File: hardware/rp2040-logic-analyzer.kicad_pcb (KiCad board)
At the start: 4 copper layers, 65 x 45 mm, 82 parts, among them J1 TYPE-C-31-M-12, J2 PROBE 2x16, J3 VREF_EXT, J4 ADC 1x3 (DNF), SW1 SK13D07VG5, SW2 TS-1187A-B-A-B, SW3 TS-1187A-B-A-B, U1 RP2040, U2 W25Q128JVSIQ, U3 TXU0104PWR, U4 TXU0104PWR, U5 TXU0104PWR, U6 TXU0104PWR, U7 AMS1117-3.3, U8 USBLC6-2SC6, X1 ABM8-272-T3 12MHz

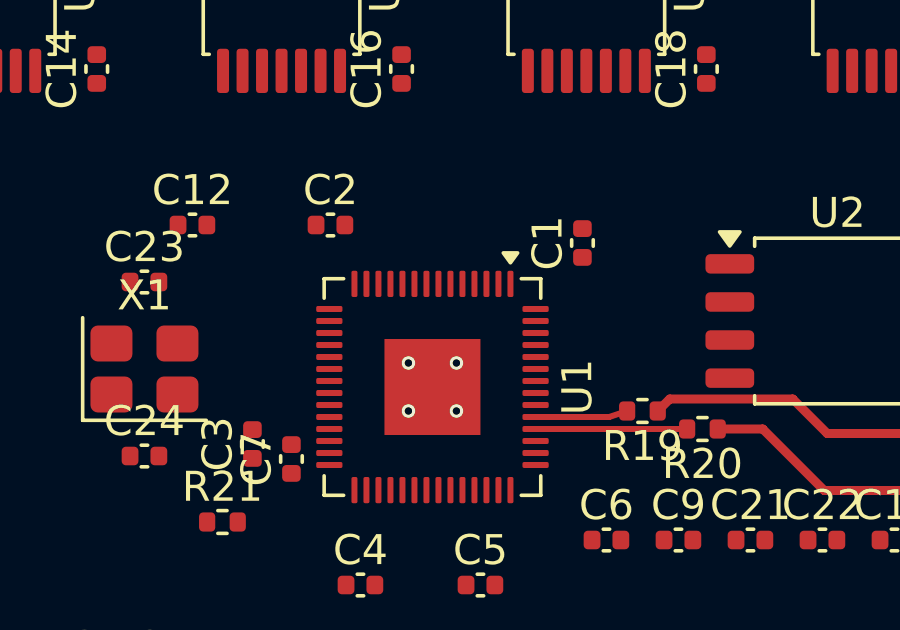
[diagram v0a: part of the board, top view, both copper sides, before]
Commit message: 人間の GUI 編集を取り込み（PCB: 微細ピッチのファンアウト配線 10 本＋ビア 5・回路図の整形）
Co-Authored-By: Claude Opus 5 (1M context) <noreply@anthropic.com>
Claude-Session: https://claude.ai/code/session_01QcyfLK5Dm75FgDGZMr6fff
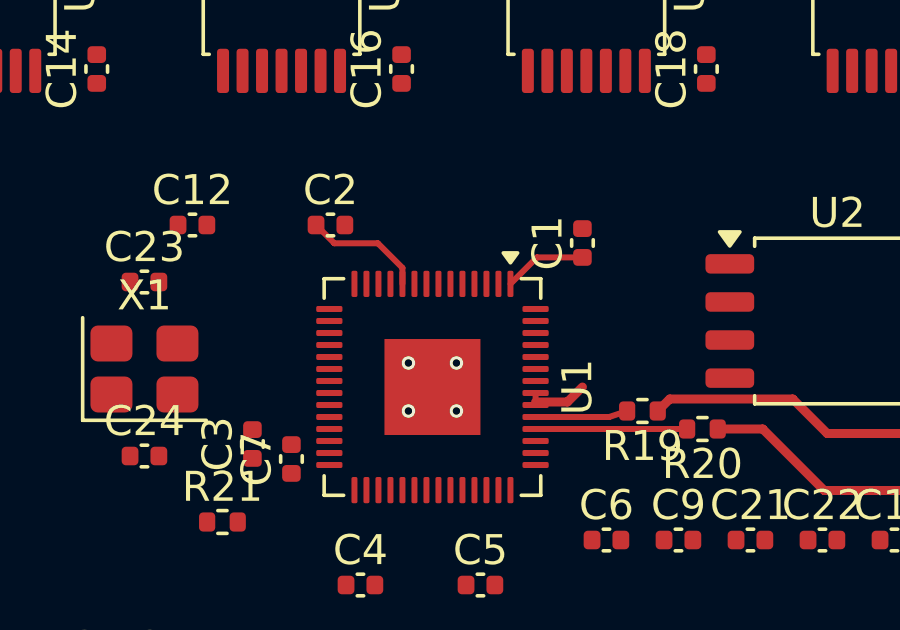
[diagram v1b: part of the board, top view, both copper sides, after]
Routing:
- net +3V3: track 0.00 -> 8.94 mm

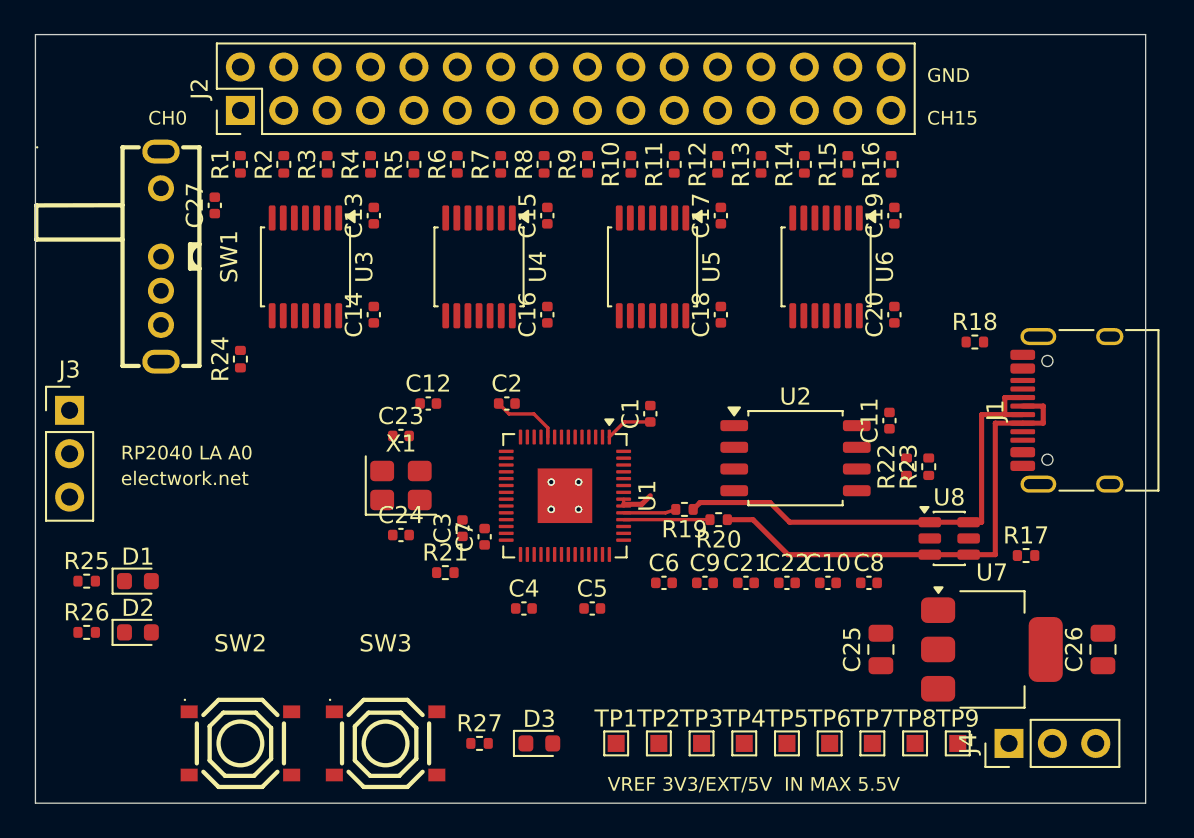
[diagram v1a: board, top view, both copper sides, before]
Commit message: PCB 配線完了（人間の GUI 作業＋補助スクリプト）: DRC error 0・未配線 0
- hardware/rp2040-logic-analyzer.kicad_pcb: 配線 778 本・ビア 182・ゾーン 5。kicad-cli drc --refill-zones --schematic-parity で error 0 / unconnected 0（warning は silk 47 件のみ・parity は TP の BOM 除外差 9 件）
- hardware/out/: 配線完了に使った補助スクリプトと記録（RESULT.md・ground-finish.md・preview）。試行物と jar は gitignore

Co-Authored-By: Claude Opus 5 (1M context) <noreply@anthropic.com>
Claude-Session: https://claude.ai/code/session_01QcyfLK5Dm75FgDGZMr6fff
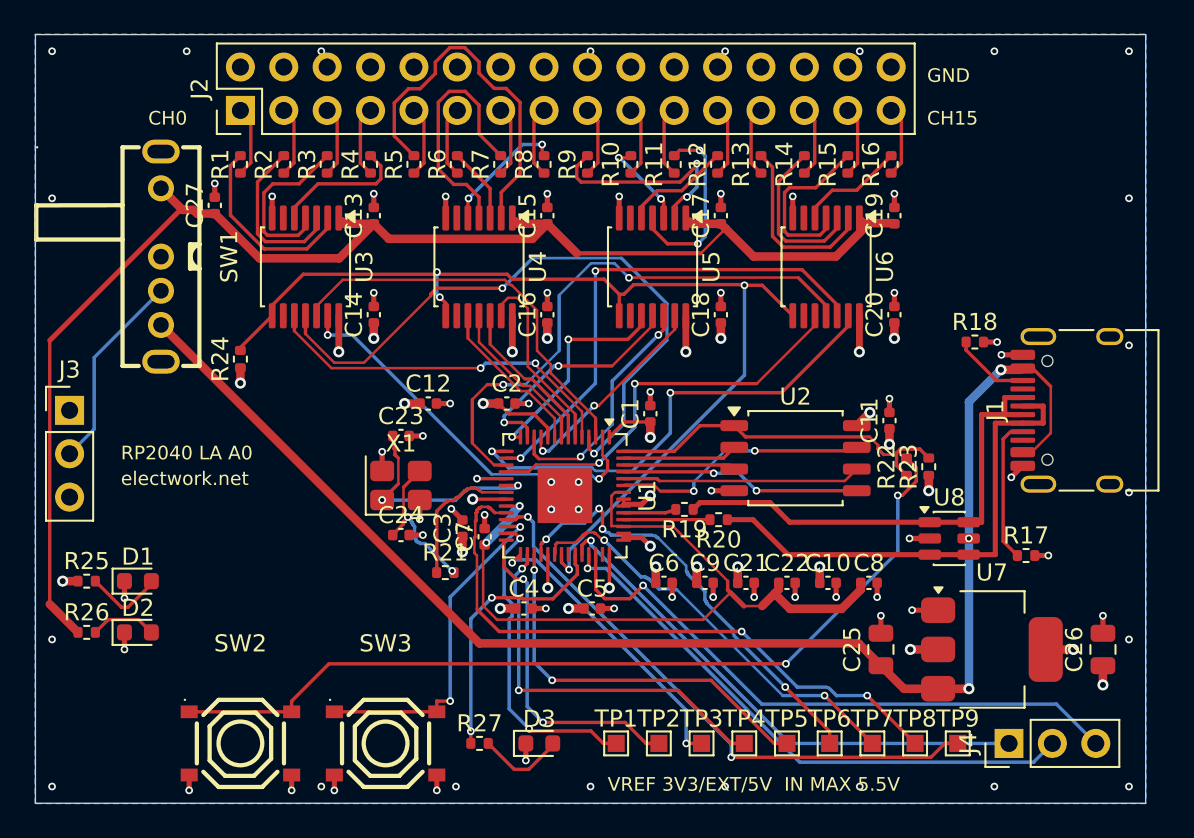
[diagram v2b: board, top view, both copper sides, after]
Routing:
- net VREF: track 0.00 -> 84.4 mm
- net +5V: track 0.00 -> 82.6 mm, vias 0 -> 3
- net /TXU_OE: track 0.00 -> 61.5 mm, vias 0 -> 4
- net /USB_BOOT: track 0.00 -> 52.1 mm, vias 0 -> 2
- net GND: track 0.00 -> 45.9 mm, vias 4 -> 74
- net /DVDD: track 0.00 -> 44.3 mm, vias 0 -> 2
- net /D2: track 0.00 -> 38.3 mm, vias 0 -> 2
- net +3V3: track 8.94 -> 47.2 mm, vias 0 -> 31
- net /SWCLK: track 0.00 -> 36.8 mm, vias 0 -> 2
- net /GP28_ADC2: track 0.00 -> 35.7 mm, vias 0 -> 1
- net /SWDIO: track 0.00 -> 33.9 mm, vias 0 -> 2
- net /GP27_ADC1: track 0.00 -> 33.2 mm, vias 0 -> 1
- net /D14: track 0.00 -> 32.0 mm, vias 0 -> 2
- net /GP26_ADC0: track 0.00 -> 30.7 mm, vias 0 -> 1
- net /D13: track 0.00 -> 28.7 mm, vias 0 -> 2
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- added copper zone on B.Cu, net GND
